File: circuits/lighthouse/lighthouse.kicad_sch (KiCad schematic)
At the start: 53 parts, among them J1 USB_C_Receptacle_USB2.0_14P, J2 Conn_01x03_Socket, Q1 S9013, Q4 SS8050, Q5 SS8050, U10 CP2102-GMR, U2 AMS1117-3.3, U7 ESP32-WROOM-32

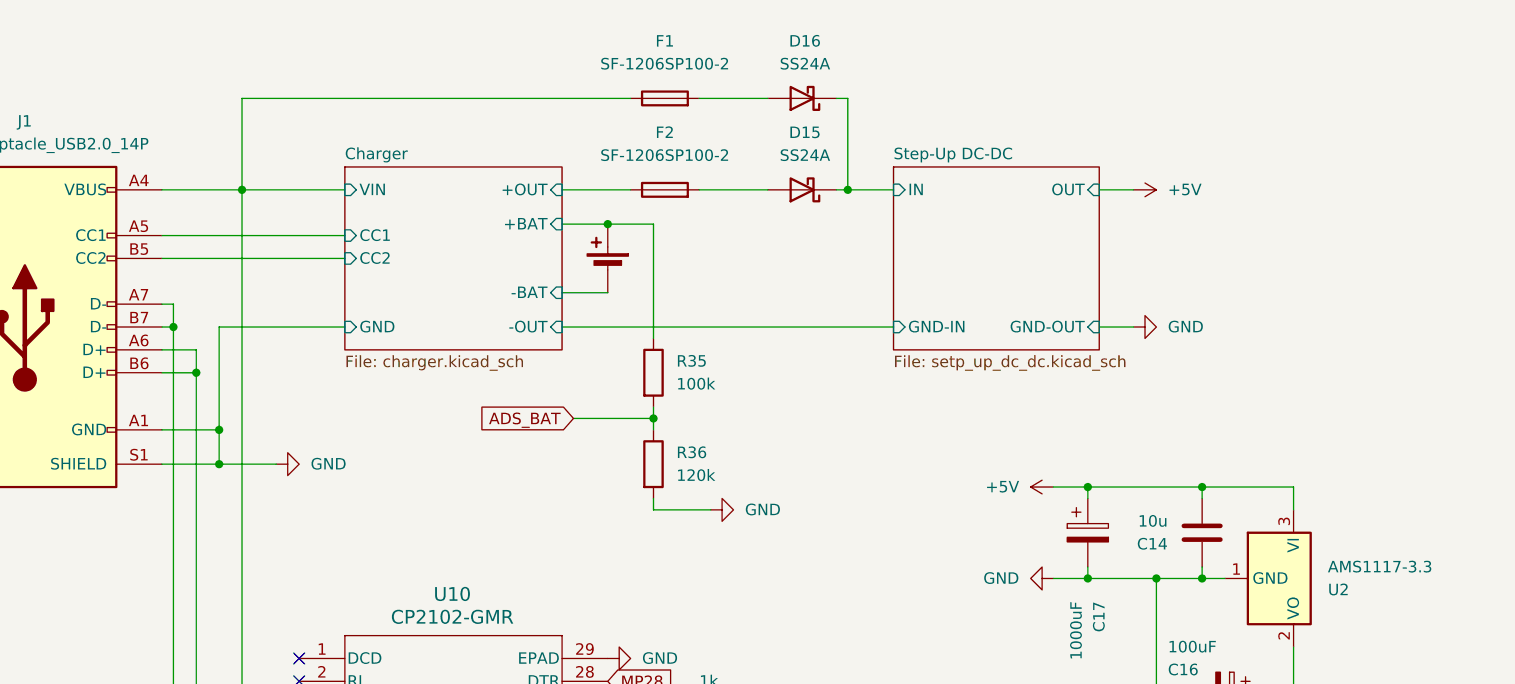
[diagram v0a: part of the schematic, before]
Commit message: Added all the models
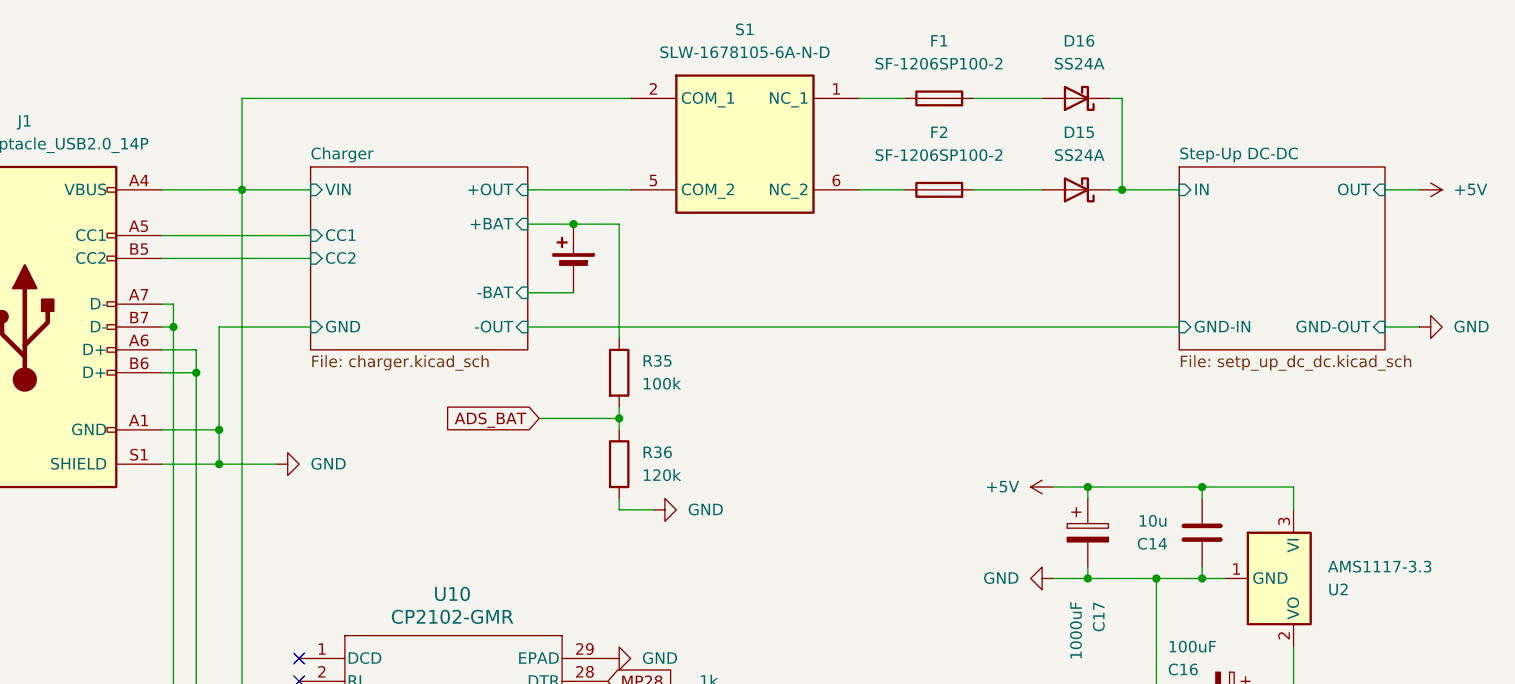
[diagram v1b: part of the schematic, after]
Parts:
- added S1: SLW-1678105-6A-N-D, SLW-1678105-6A-N-D:SLW16781056AND, symbol SLW-1678105-6A-N-D:SLW-1678105-6A-N-D
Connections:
- net Charger/+OUT: now also S1.5 (COM_2); no longer F2.1
- net Charger/VIN: now also S1.2 (COM_1); no longer F1.1
- new net: F2.1, S1.6 (NC_2)
- new net: F1.1, S1.1 (NC_1)
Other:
- moved on the sheet: D15, D16, F1, F2, R35, R36

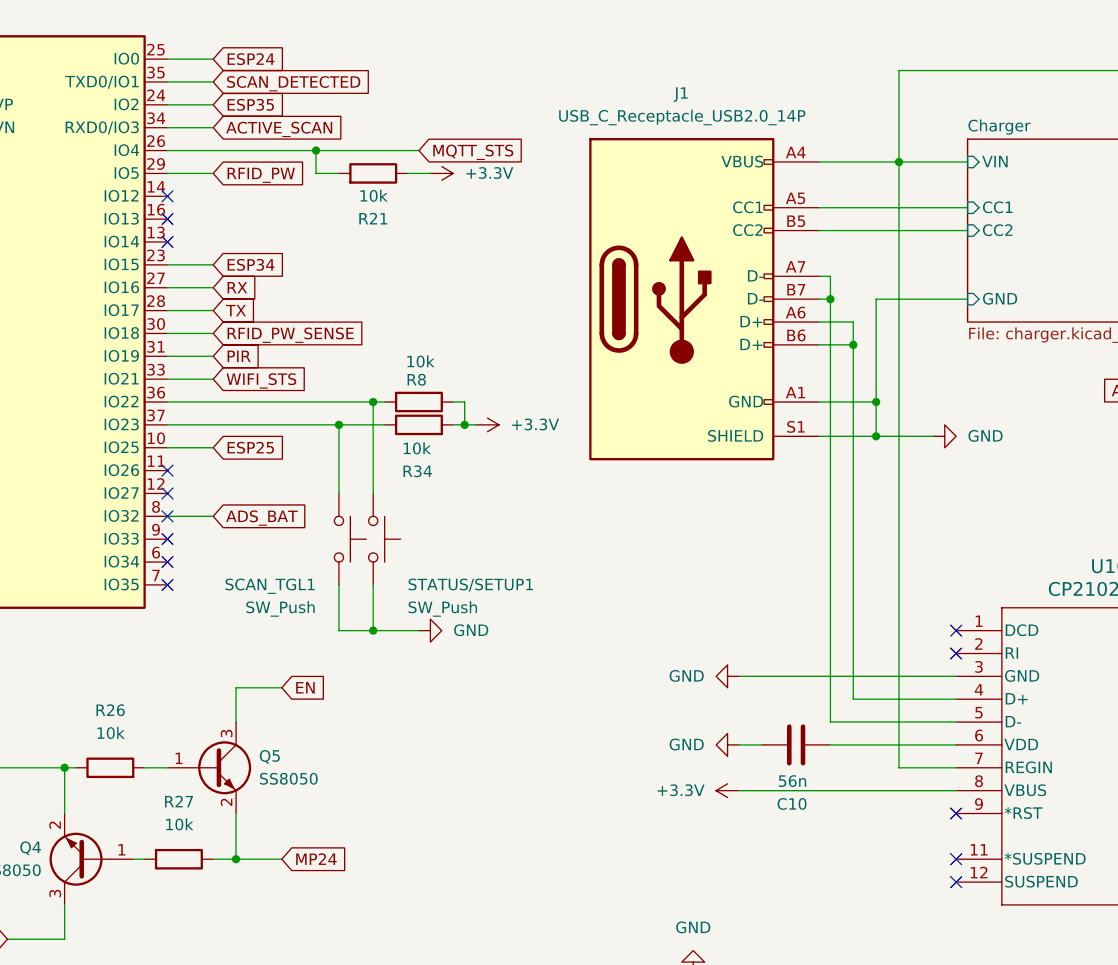
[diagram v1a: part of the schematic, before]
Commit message: Added usb power sense to schematic, pcb pending
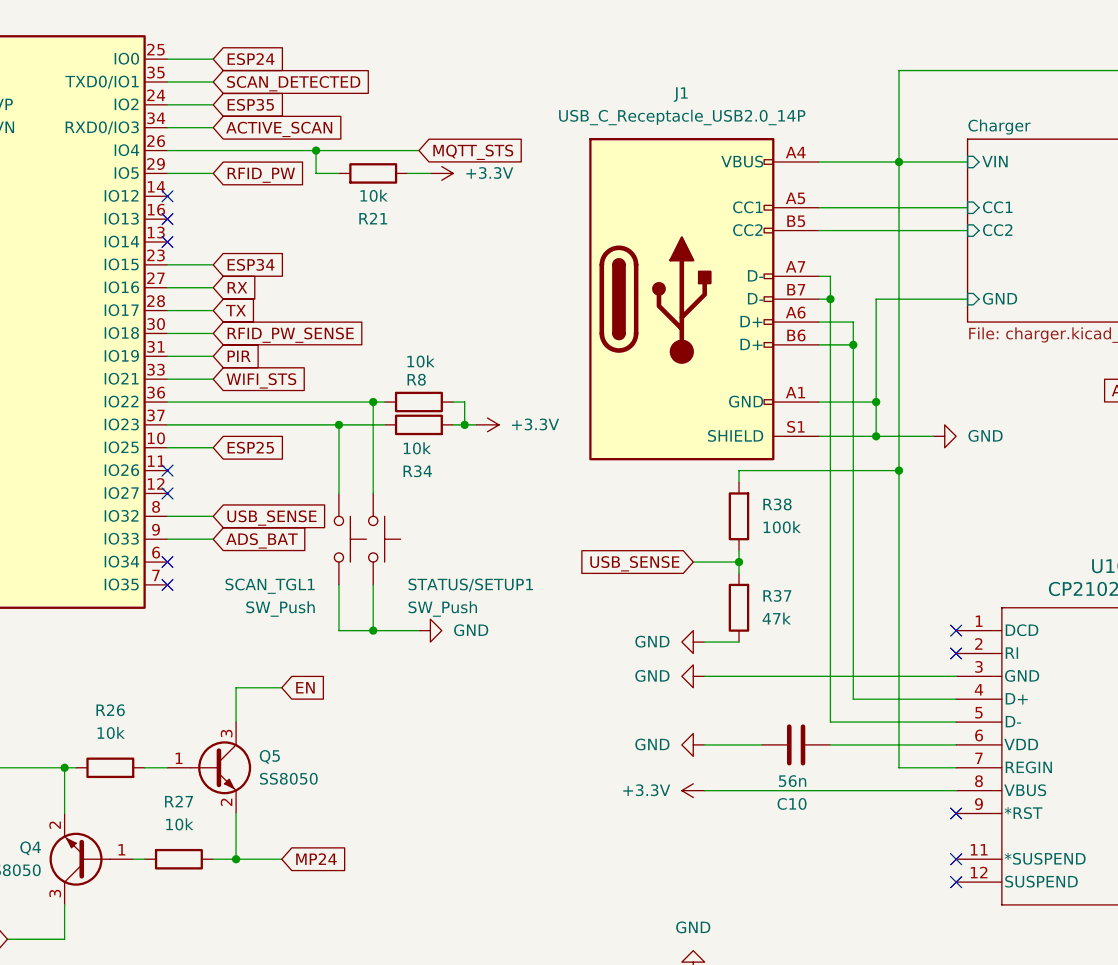
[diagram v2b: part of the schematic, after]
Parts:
- added R37: 47k, Resistor_SMD:R_1206_3216Metric_Pad1.30x1.75mm_HandSolder, symbol Device:R
- added R38: 100k, Resistor_SMD:R_1206_3216Metric_Pad1.30x1.75mm_HandSolder, symbol Device:R
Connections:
- net ADS_BAT: now also U7.9 (IO33); no longer U7.8 (IO32)
- net Charger/VIN: now also R38.2
- net GND: now also R37.1
- new net USB_SENSE: R37.2, R38.1, U7.8 (IO32)
- no-connect marks 25 -> 23

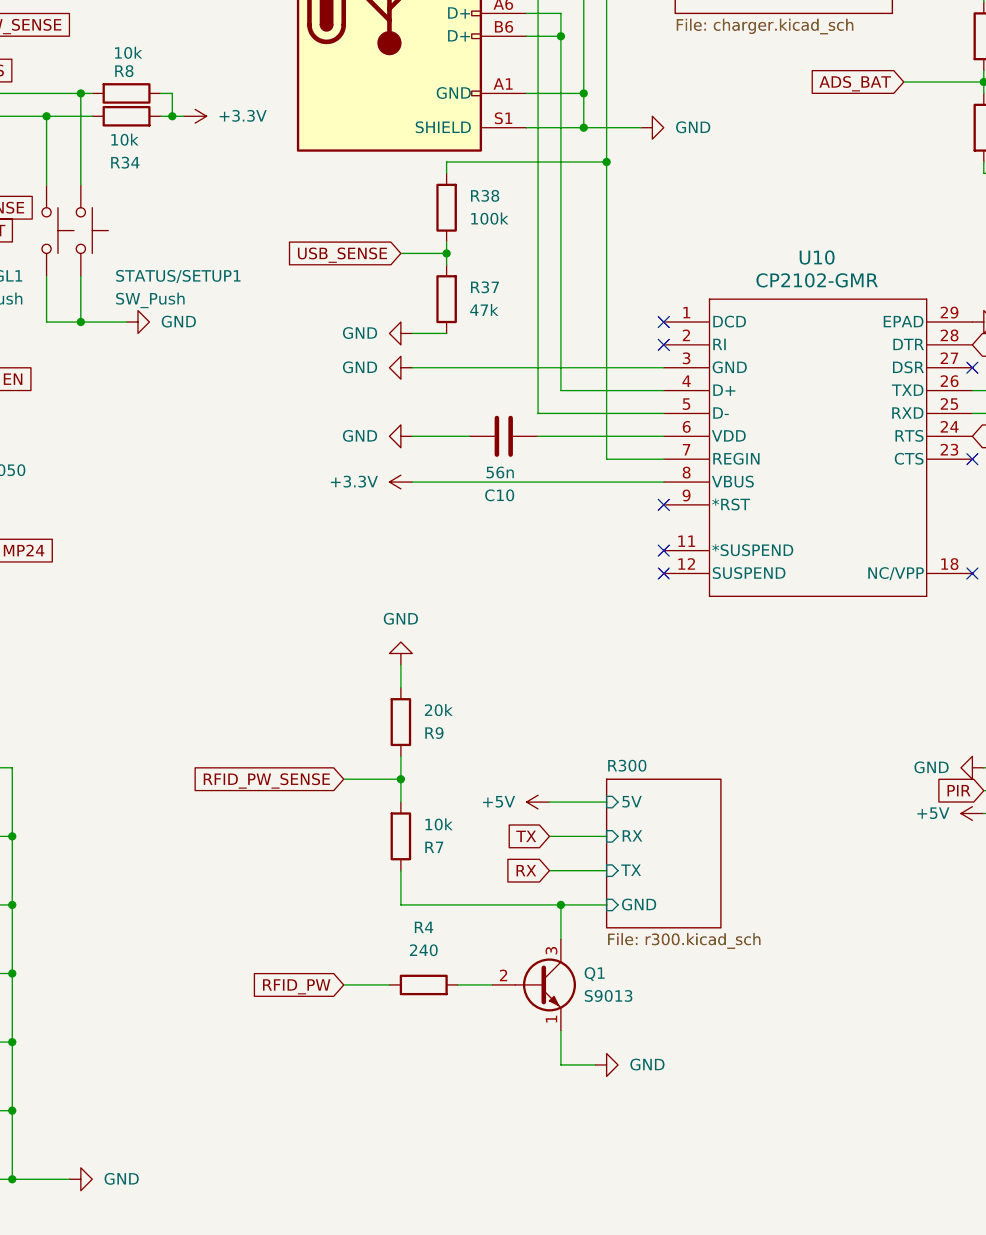
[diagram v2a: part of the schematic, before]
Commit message: Removed silkscreen numbering
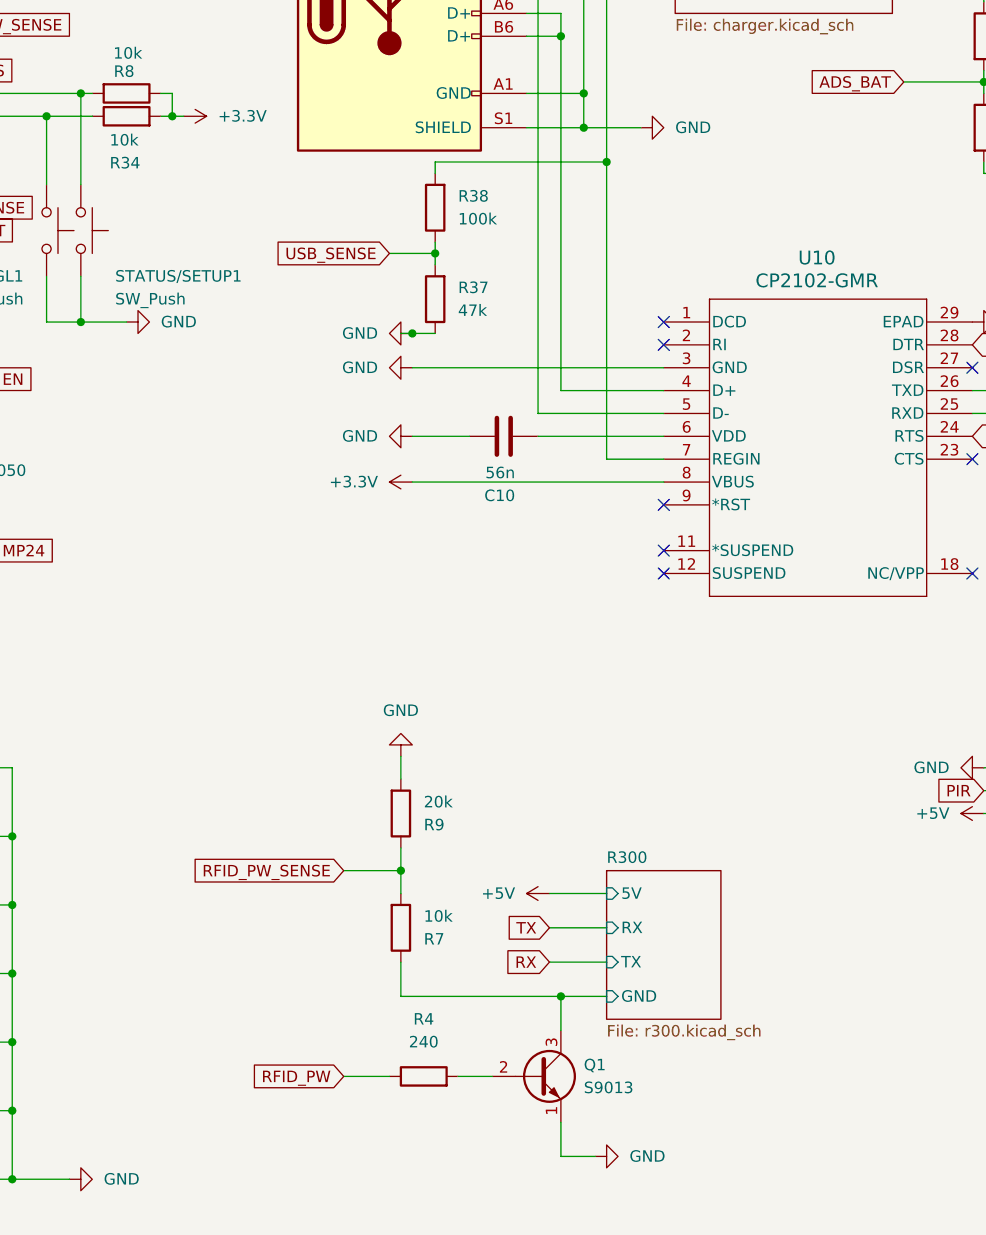
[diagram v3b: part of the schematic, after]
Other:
- moved on the sheet: Q1, R37, R38, R4, R7, R9
